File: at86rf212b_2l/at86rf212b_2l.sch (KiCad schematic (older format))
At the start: 23 parts, among them J1 Conn_Coaxial, J2 Conn_01x07, J3 Conn_01x07, U1 AT86RF212B, Y1 16.0Mhz

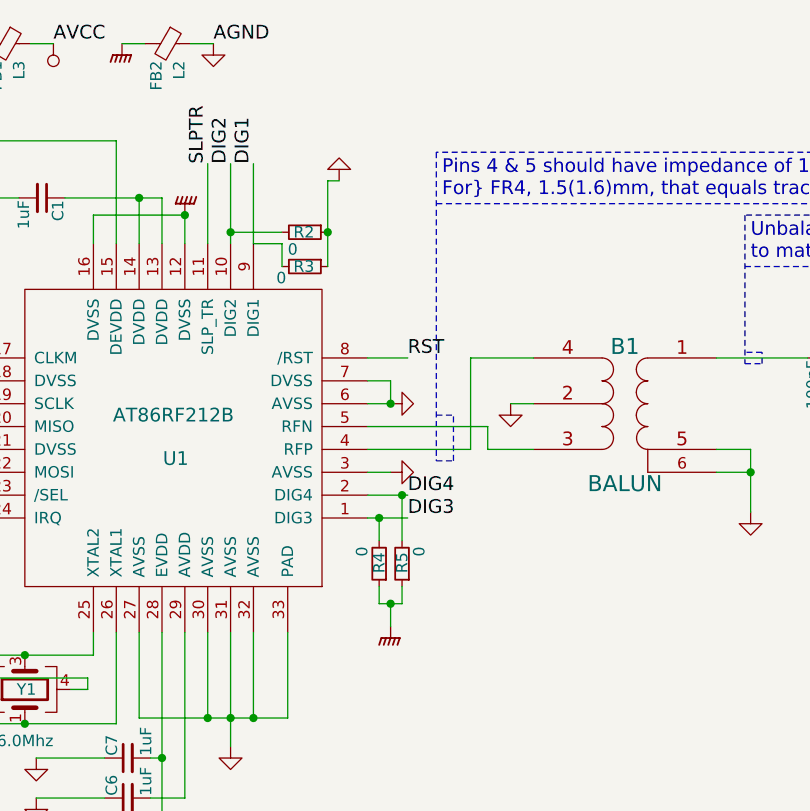
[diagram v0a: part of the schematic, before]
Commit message: Fix the Analog and Digital Ground connections for pins DIG1,DIG2,DIG3,DIG4. Were swapped in the previous version
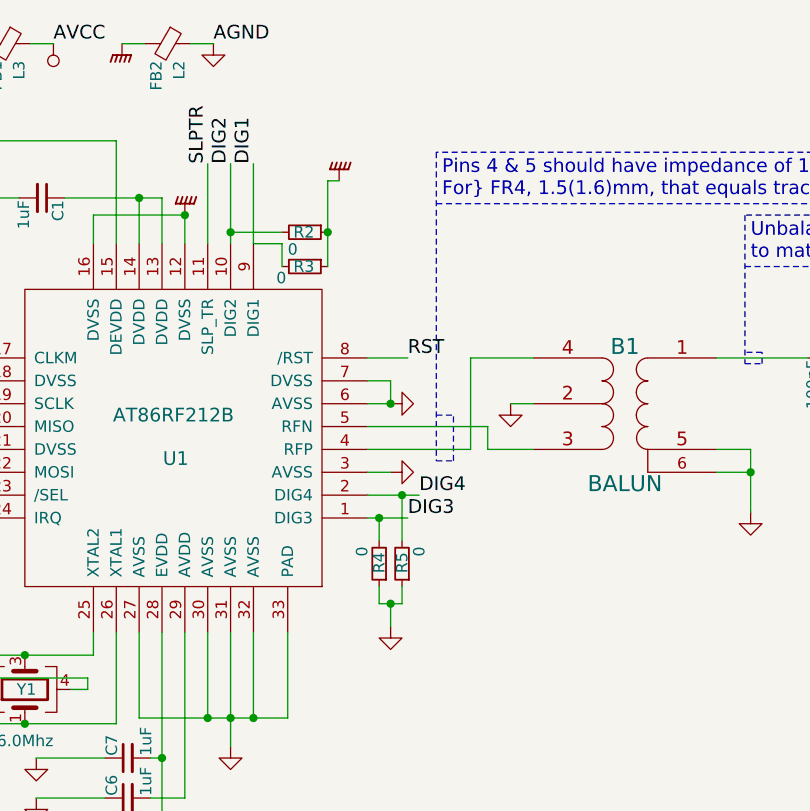
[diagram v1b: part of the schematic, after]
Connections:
- net GND: now also R4.1, R5.1; no longer R2.1, R3.1
- net GNDPWR: now also R2.1, R3.1; no longer R4.1, R5.1
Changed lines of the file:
@@
 L GND #PWR013
 U 1 1 59E9D9C6
-P 2875 1150
-F 0 "#PWR013" H 2875 1200 30  0001 C CNN
-F 1 "GND" H 2875 1025 30  0001 C CNN
-F 2 "" H 2875 1150 60  0000 C CNN
-F 3 "" H 2875 1150 60  0000 C CNN
-	1    2875 1150
-	1    0    0    1
+P 3100 3100
+F 0 "#PWR013" H 3100 3150 30  0001 C CNN
+F 1 "GND" H 3100 2975 30  0001 C CNN
+F 2 "" H 3100 3100 60  0000 C CNN
+F 3 "" H 3100 3100 60  0000 C CNN
+	1    3100 3100
+	-1   0    0    -1
 $EndComp
 Wire Wire Line
@@
 	3000 2625 3175 2625
 Wire Wire Line
-	3000 2525 3175 2525
-Text Label 3175 2525 0    60   ~ 0
+	3000 2525 3225 2525
+Text Label 3225 2525 0    60   ~ 0
 DIG4
 Text Label 3175 2625 0    60   ~ 0
@@
 L GNDPWR #PWR022
 U 1 1 59EA195A
-P 3100 3100
-F 0 "#PWR022" H 3100 3150 30  0001 C CNN
-F 1 "GNDPWR" H 3100 2975 30  0001 C CNN
-F 2 "" H 3100 3050 60  0000 C CNN
-F 3 "" H 3100 3050 60  0000 C CNN
-	1    3100 3100
-	1    0    0    -1
-$EndComp
-$Comp
+P 2875 1150
+F 0 "#PWR022" H 2875 1200 30  0001 C CNN
+F 1 "GNDPWR" H 2875 1025 30  0001 C CNN
+F 2 "" H 2875 1100 60  0000 C CNN
+F 3 "" H 2875 1100 60  0000 C CNN
+	1    2875 1150
+	-1   0    0    1
+$EndComp
+$Comp

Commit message: AT86RFR212b package, mistakenly used QFP instaed of the proper QFN 32 bit package. Now fixed. That lead to some minor tweaks and fixes around the ground planes. Also moved the resistor for the IRQ, everything else is the same. Tracks are reduced to 0.2mm, as our manufacturing company is producing those without a problem and we also have 0.1mm tracks for the antenna feed lines, so there is no change of price. Also tweaked the pad design rules for the solder paste mask. You will see the plots. Missing is the SVG for the mask, but that will come later. Components are here, BOM to follow shortly.
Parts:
- U1: footprint Housings_QFP:LQFP-32-1EP_5x5mm_Pitch0.5mm -> Housings_DFN_QFN:QFN-32-1EP_5x5mm_Pitch0.5mm
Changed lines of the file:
@@
 F 0 "U1" H 2140 2365 60  0000 C CNN
 F 1 "AT86RF212B" H 2150 2175 60  0000 C CNN
-F 2 "Housings_QFP:LQFP-32-1EP_5x5mm_Pitch0.5mm" H 2150 2275 60  0001 C CNN
+F 2 "Housings_DFN_QFN:QFN-32-1EP_5x5mm_Pitch0.5mm" H 2150 2275 60  0001 C CNN
 F 3 "" H 2150 2275 60  0001 C CNN
 	1    2150 2275
